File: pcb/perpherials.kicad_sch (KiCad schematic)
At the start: 9 parts, among them J5 050700622, U7 M24C64-FCS6TP/K, U8 BNO055

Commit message: Address OEPS manufacturing concerns
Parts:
- J5: now in the parts list
- J?: now left out of the parts list
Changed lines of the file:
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@@
   )
   (symbol (lib_id "jonnew:Conn_02x3_Odd_Even_4Mech") (at 214.63 125.73 0) (unit 1)
-    (in_bom no) (on_board yes) (dnp no)
+    (in_bom yes) (on_board yes) (dnp no)
     (property "Reference" "J5" (at 214.63 114.3 0)
       (effects (font (size 1.27 1.27)))
@@
   )
   (symbol (lib_id "Connector_Generic:Conn_02x05_Odd_Even") (at 96.52 58.42 0) (unit 1)
-    (in_bom yes) (on_board yes) (dnp yes) (fields_autoplaced)
+    (in_bom no) (on_board yes) (dnp yes) (fields_autoplaced)
     (property "Reference" "J?" (at 97.79 46.99 0)
       (effects (font (size 1.27 1.27)))

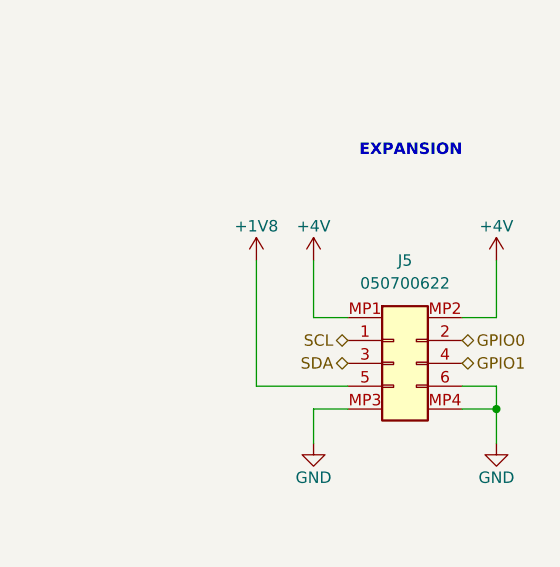
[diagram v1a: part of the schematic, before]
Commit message: More fixes after OEPS feedback
- BOM update
- Remove CSV gitignore rule
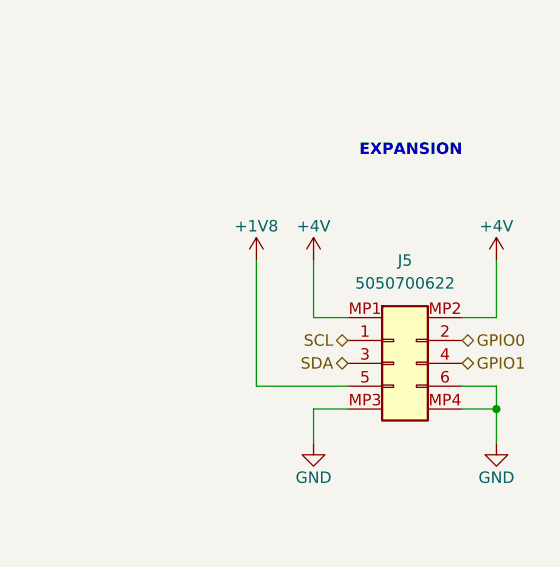
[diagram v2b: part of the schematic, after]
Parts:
- J5: value 050700622 -> 5050700622
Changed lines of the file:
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@@
       (effects (font (size 1.27 1.27)))
     )
-    (property "Value" "050700622" (at 214.63 116.84 0)
+    (property "Value" "5050700622" (at 214.63 116.84 0)
       (effects (font (size 1.27 1.27)))
     )

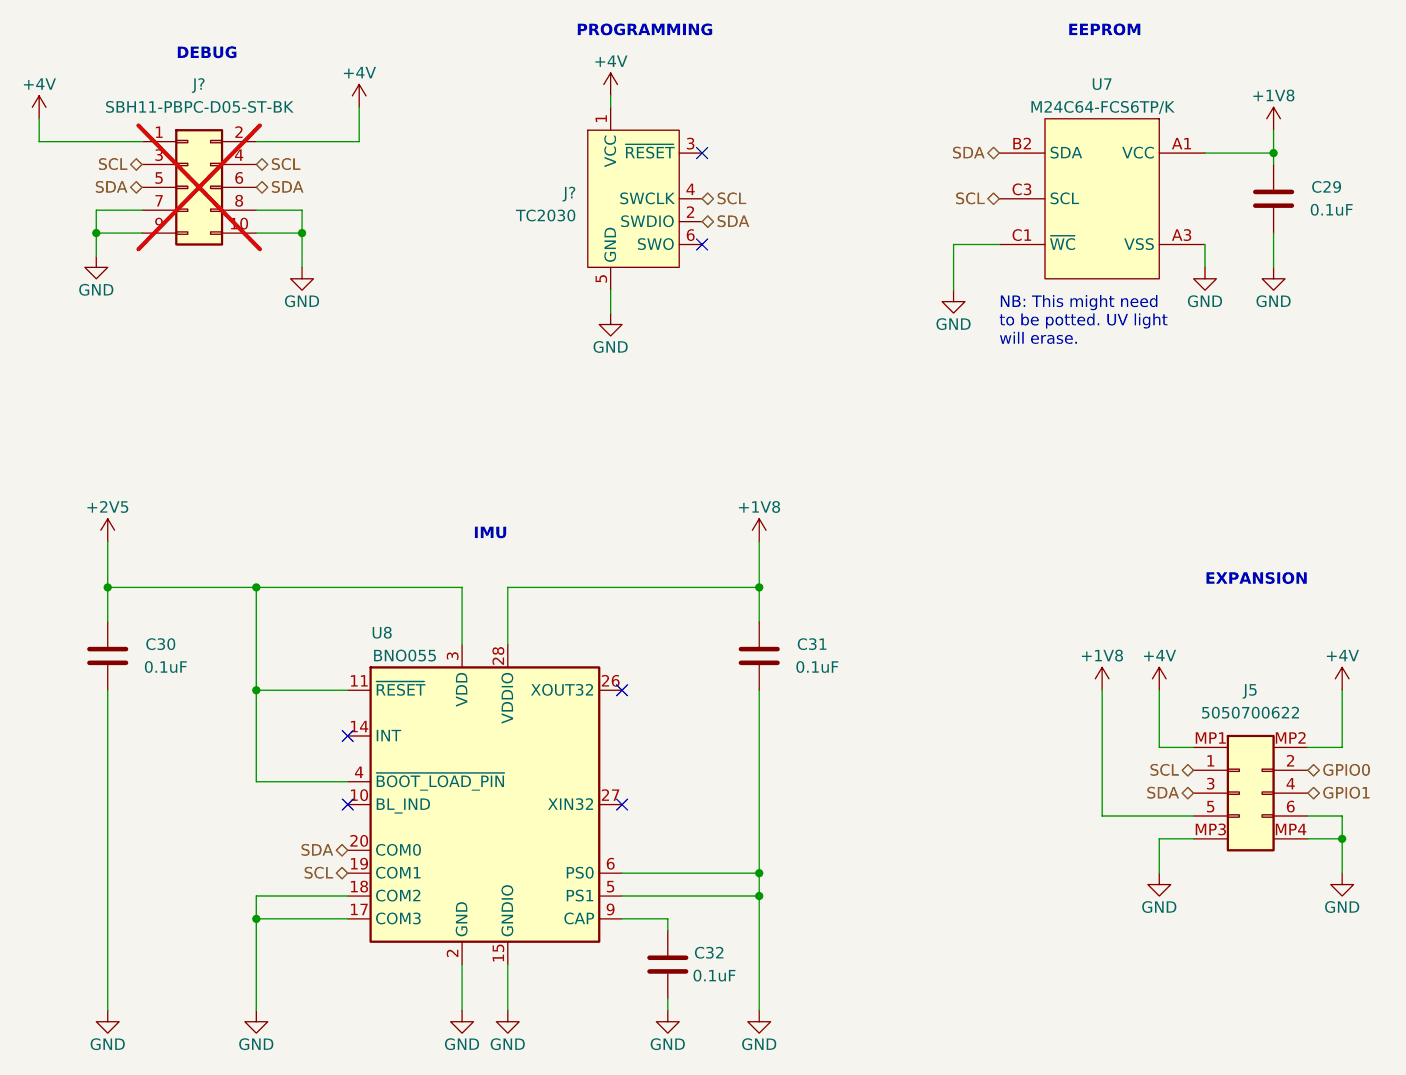
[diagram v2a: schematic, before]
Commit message: Redo NP Power circuit
- For NP 1.0, separate 1.8 and 1.2 rails are needed for digital and
analog sections, respectively, with a delay between power on. This has
been addressed here
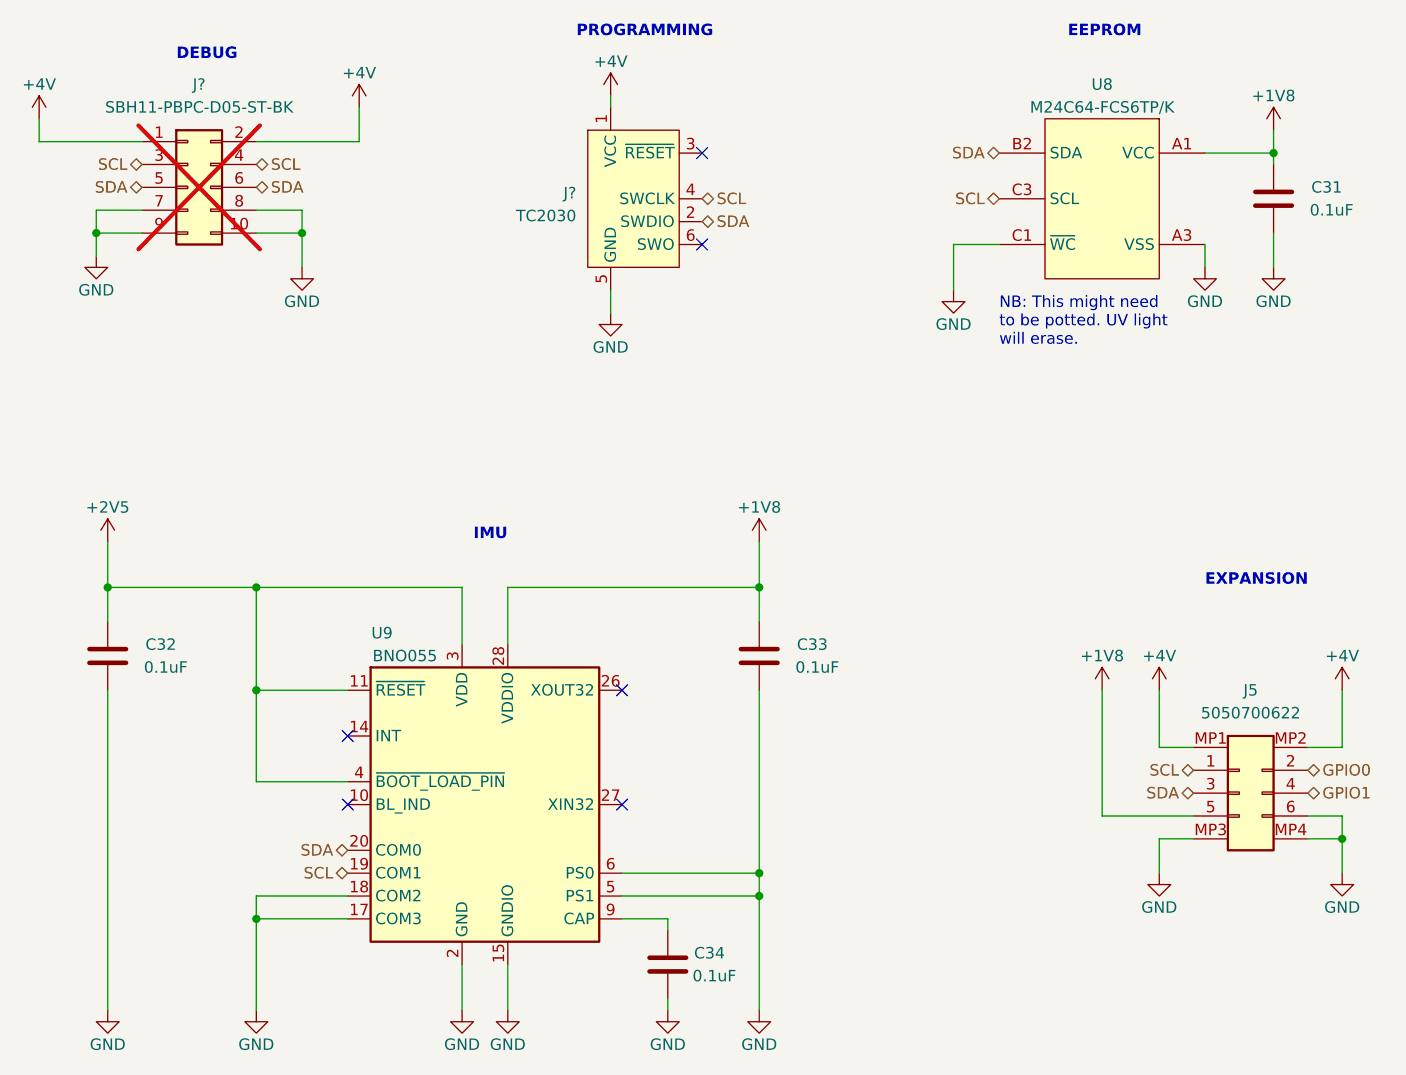
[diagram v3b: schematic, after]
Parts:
- renumbered C29 to C31, C30 to C32, C31 to C33, C32 to C34, U7 to U8, U8 to U9

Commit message: Revision B
- Tiny changes after testing revision A. Really may not be needed other
than POR chip part number changes (same footprint, different threshold
voltage) and even that is not really needed.
- Fixed mislabelled test point silkscreen
- Added extra 10uF cap to Vcoax
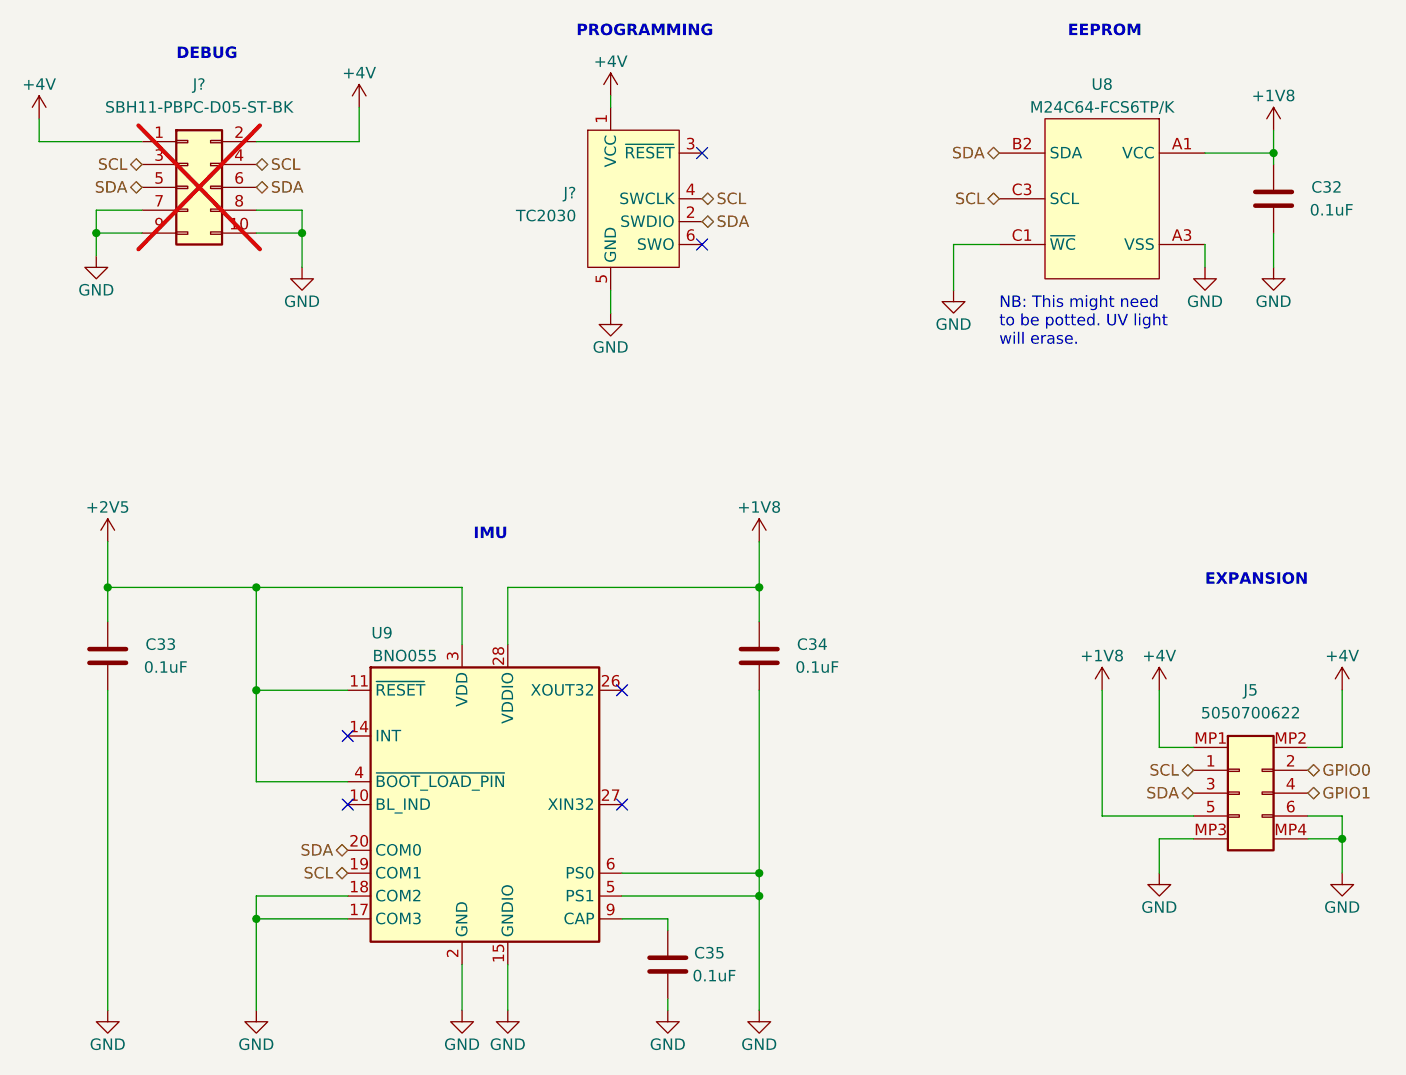
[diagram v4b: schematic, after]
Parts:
- renumbered C31 to C32, C32 to C33, C33 to C34, C34 to C35
